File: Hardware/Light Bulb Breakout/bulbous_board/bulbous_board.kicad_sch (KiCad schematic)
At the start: 4 parts, among them Q1 NMOS, U1 Teensy4.1_DEV-16771

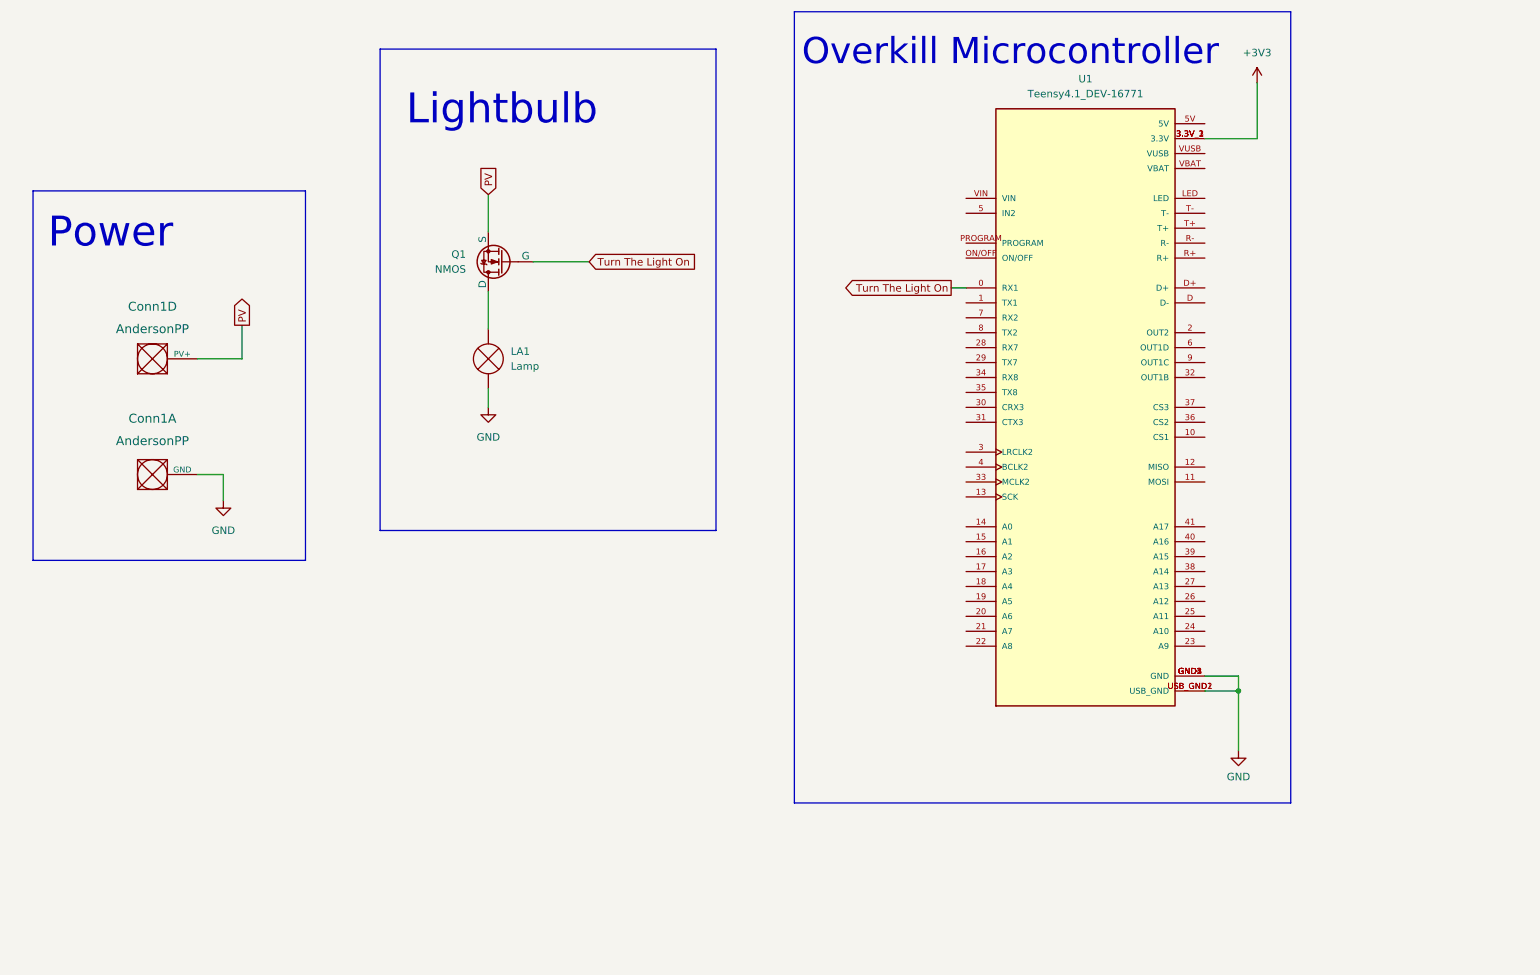
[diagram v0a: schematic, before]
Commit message: Amogus
Found out it is not a good idea to put 12 volts into the teensy and that's why we need an OKI. Also 2 pin connectors are a thing.
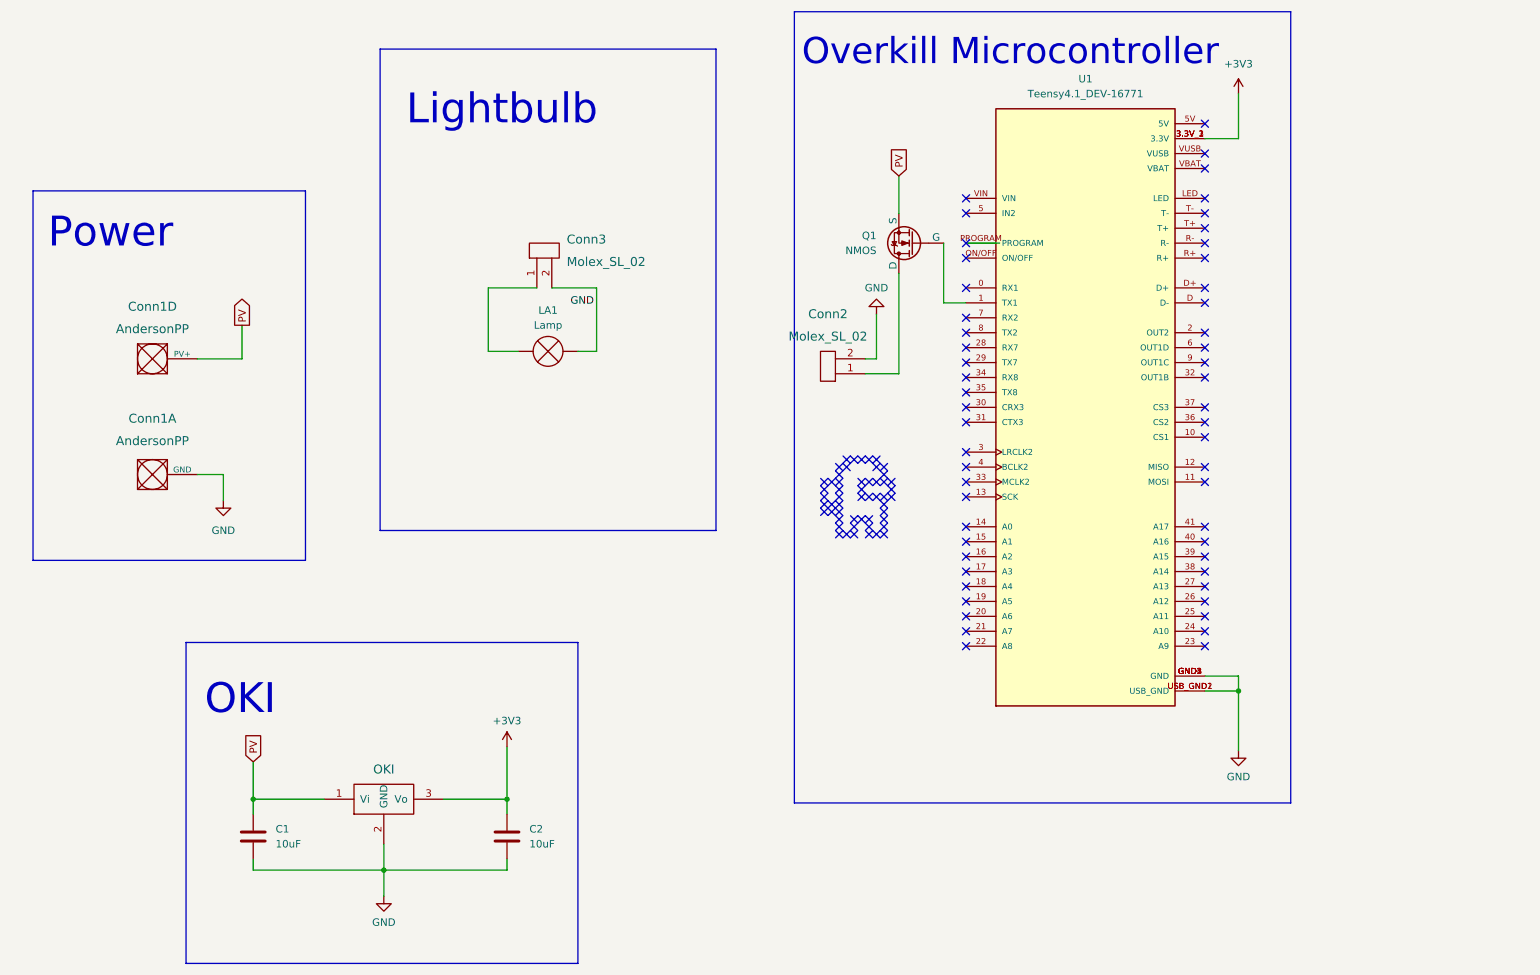
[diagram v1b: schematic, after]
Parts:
- added C1, C2: 10uF, Capacitor_SMD:C_0603_1608Metric_Pad1.08x0.95mm_HandSolder, symbol Device:C
- added Conn2, Conn3: Molex_SL_02, symbol MRDT_Connectors:Molex_SL_02
- added U2: OKI, MRDT_Devices:OKI_Horizontal, symbol MRDT_Devices:OKI
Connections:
- net +3V3: now also C2.1, U2.3 (Vo)
- net GND: now also C1.2, C2.2, Conn2.2, U2.2 (GND); no longer LA1.1 (-)
- net PV: now also C1.1, U2.1 (Vi)
- net at LA1.2 (+): now also Conn3.1; no longer Q1.1 (D)
- net at U1.1 (TX1): now also Q1.2 (G)
- net Turn The Light On: no longer names the net of U1.0 (RX1)
- net Turn The Light On: no longer Q1.2 (G)
- new net: Conn3.2, LA1.1 (-)
- new net: Conn2.1, Q1.1 (D)
- no-connect marks 0 -> 107
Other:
- note added: "OKI"
- moved on the sheet: LA1

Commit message: Amogus round 2
fixed a label because Derw said it was bad
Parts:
- removed unit 4 of Conn1
- added unit 5 of Conn1
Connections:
- net GND: now also Conn3.2, LA1.1 (-)
- net PV renamed +12V
- net +12V: now also Conn1.1
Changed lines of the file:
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@@
+    (stroke (width 0) (type default))
+  )
+  (wire (pts (xy 120.015 76.835) (xy 123.19 76.835))
     (stroke (width 0) (type default))
   )
@@
     (stroke (width 0) (type default))
   )
-  (wire (pts (xy 120.015 76.835) (xy 123.19 76.835))
+  (wire (pts (xy 76.835 153.035) (xy 64.77 153.035))
+    (stroke (width 0) (type default))
+  )
+  (wire (pts (xy 107.95 155.575) (xy 107.95 153.035))
+    (stroke (width 0) (type default))
+  )
+  (wire (pts (xy 123.19 76.835) (xy 123.19 66.04))
     (stroke (width 0) (type default))
   )
   (wire (pts (xy 55.245 78.105) (xy 62.865 78.105))
-    (stroke (width 0) (type default))
-  )
-  (wire (pts (xy 76.835 153.035) (xy 64.77 153.035))
-    (stroke (width 0) (type default))
-  )
-  (wire (pts (xy 107.95 155.575) (xy 107.95 153.035))
-    (stroke (width 0) (type default))
-  )
-  (wire (pts (xy 123.19 76.835) (xy 123.19 66.04))
     (stroke (width 0) (type default))
   )
@@
     (effects (font (size 5.08 5.08)) (justify left bottom))
   )
-  (label "GND" (at 118.745 69.215 0) (fields_autoplaced)
+  (label "GND" (at 115.57 66.04 0) (fields_autoplaced)
     (effects (font (size 1.27 1.27)) (justify left bottom))
   )
-  (global_label "PV" (shape input) (at 174.625 46.99 90) (fields_autoplaced)
-    (effects (font (size 1.27 1.27)) (justify left))
-    (property "Intersheetrefs" "${INTERSHEET_REFS}" (at 174.625 42.1465 90)
-      (effects (font (size 1.27 1.27)) (justify left) hide)
-    )
-  )
-  (global_label "PV" (shape output) (at 62.865 72.39 90) (fields_autoplaced)
-    (effects (font (size 1.27 1.27)) (justify left))
-    (property "Intersheetrefs" "${INTERSHEET_REFS}" (at 62.865 67.5465 90)
-      (effects (font (size 1.27 1.27)) (justify left) hide)
-    )
-  )
-  (global_label "PV" (shape input) (at 64.77 146.685 90) (fields_autoplaced)
-    (effects (font (size 1.27 1.27)) (justify left))
-    (property "Intersheetrefs" "${INTERSHEET_REFS}" (at 64.77 141.3412 90)
-      (effects (font (size 1.27 1.27)) (justify left) hide)
-    )
-  )
-  (symbol (lib_id "MRDT_Connectors:AndersonPP") (at 45.085 80.645 0) (unit 4)
-    (in_bom yes) (on_board yes) (dnp no) (fields_autoplaced)
-    (property "Reference" "Conn1" (at 47.625 69.215 0)
-      (effects (font (size 1.524 1.524)))
-    )
-    (property "Value" "AndersonPP" (at 47.625 73.025 0)
-      (effects (font (size 1.524 1.524)))
-    )
-    (property "Footprint" "" (at 41.275 94.615 0)
-      (effects (font (size 1.524 1.524)) hide)
-    )
-    (property "Datasheet" "" (at 41.275 94.615 0)
-      (effects (font (size 1.524 1.524)) hide)
-    )
-    (pin "1")
-    (pin "2")
-    (pin "3")
-    (pin "4")
-    (pin "1")
-    (instances
-      (project "bulbous_board"
-        (path "/049c3f09-c046-40c3-9872-e62b40667976"
-          (reference "Conn1") (unit 4)
+  (symbol (lib_id "power:+12V") (at 64.77 146.685 0) (unit 1)
+    (in_bom yes) (on_board yes) (dnp no) (fields_autoplaced)
+    (property "Reference" "#PWR09" (at 64.77 150.495 0)
+      (effects (font (size 1.27 1.27)) hide)
+    )
+    (property "Value" "+12V" (at 64.77 142.24 0)
+      (effects (font (size 1.27 1.27)))
+    )
+    (property "Footprint" "" (at 64.77 146.685 0)
+      (effects (font (size 1.27 1.27)) hide)
+    )
+    (property "Datasheet" "" (at 64.77 146.685 0)
+      (effects (font (size 1.27 1.27)) hide)
+    )
+    (pin "1")
+    (instances
+      (project "bulbous_board"
+        (path "/049c3f09-c046-40c3-9872-e62b40667976"
+          (reference "#PWR09") (unit 1)
         )
       )
@@
     )
   )
+  (symbol (lib_id "power:+12V") (at 62.865 72.39 0) (unit 1)
+    (in_bom yes) (on_board yes) (dnp no) (fields_autoplaced)
+    (property "Reference" "#PWR01" (at 62.865 76.2 0)
+      (effects (font (size 1.27 1.27)) hide)
+    )
+    (property "Value" "+12V" (at 62.865 67.31 0)
+      (effects (font (size 1.27 1.27)))
+    )
+    (property "Footprint" "" (at 62.865 72.39 0)
+      (effects (font (size 1.27 1.27)) hide)
+    )
+    (property "Datasheet" "" (at 62.865 72.39 0)
+      (effects (font (size 1.27 1.27)) hide)
+    )
+    (pin "1")
+    (instances
+      (project "bulbous_board"
+        (path "/049c3f09-c046-40c3-9872-e62b40667976"
+          (reference "#PWR01") (unit 1)
+        )
+      )
+    )
+  )
   (symbol (lib_id "Device:C") (at 107.95 159.385 0) (unit 1)
     (in_bom yes) (on_board yes) (dnp no) (fields_autoplaced)
@@
         (path "/88af529a-d884-4361-9125-c50b314779b3"
           (reference "C2") (unit 1)
+        )
+      )
+    )
+  )
+  (symbol (lib_id "MRDT_Connectors:AndersonPP") (at 45.085 80.645 0) (unit 5)
+    (in_bom yes) (on_board yes) (dnp no) (fields_autoplaced)
+    (property "Reference" "Conn1" (at 47.625 68.58 0)
+      (effects (font (size 1.524 1.524)))
+    )
+    (property "Value" "AndersonPP" (at 47.625 72.39 0)
+      (effects (font (size 1.524 1.524)))
+    )
+    (property "Footprint" "" (at 41.275 94.615 0)
+      (effects (font (size 1.524 1.524)) hide)
+    )
+    (property "Datasheet" "" (at 41.275 94.615 0)
+      (effects (font (size 1.524 1.524)) hide)
+    )
+    (pin "1")
+    (pin "2")
+    (pin "3")
+    (pin "4")
+    (pin "1")
+    (instances
+      (project "bulbous_board"
+        (path "/049c3f09-c046-40c3-9872-e62b40667976"
+          (reference "Conn1") (unit 5)
         )
       )
@@
         )
       )
+    )
+  )
+  (symbol (lib_id "power:+12V") (at 174.625 46.99 0) (unit 1)
+    (in_bom yes) (on_board yes) (dnp no) (fields_autoplaced)
+    (property "Reference" "#PWR08" (at 174.625 50.8 0)
+      (effects (font (size 1.27 1.27)) hide)
+    )
+    (property "Value" "+12V" (at 174.625 42.545 0)
+      (effects (font (size 1.27 1.27)))
+    )
+    (property "Footprint" "" (at 174.625 46.99 0)
+      (effects (font (size 1.27 1.27)) hide)
+    )
+    (property "Datasheet" "" (at 174.625 46.99 0)
+      (effects (font (size 1.27 1.27)) hide)
+    )
+    (pin "1")
+    (instances
+      (project "bulbous_board"
+        (path "/049c3f09-c046-40c3-9872-e62b40667976"
+          (reference "#PWR08") (unit 1)
+        )
+      )

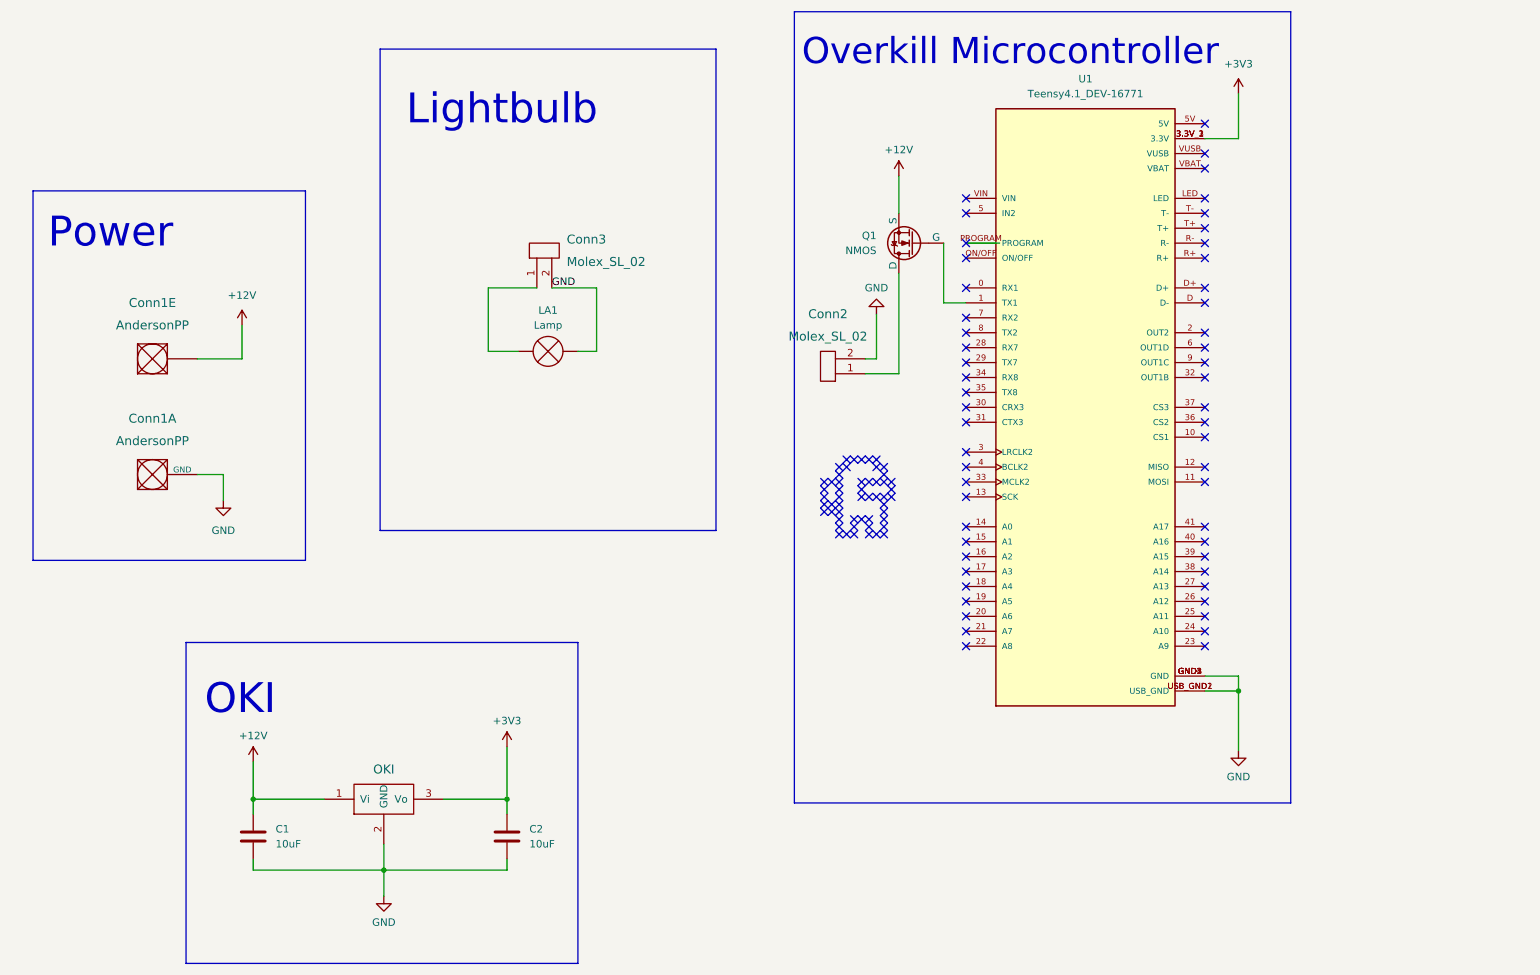
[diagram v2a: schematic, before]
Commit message: Created Stepper Symbol
TMC2208 Stepper Motor Driver and supporting circuitry.

Drew made me delete the amogus :,(
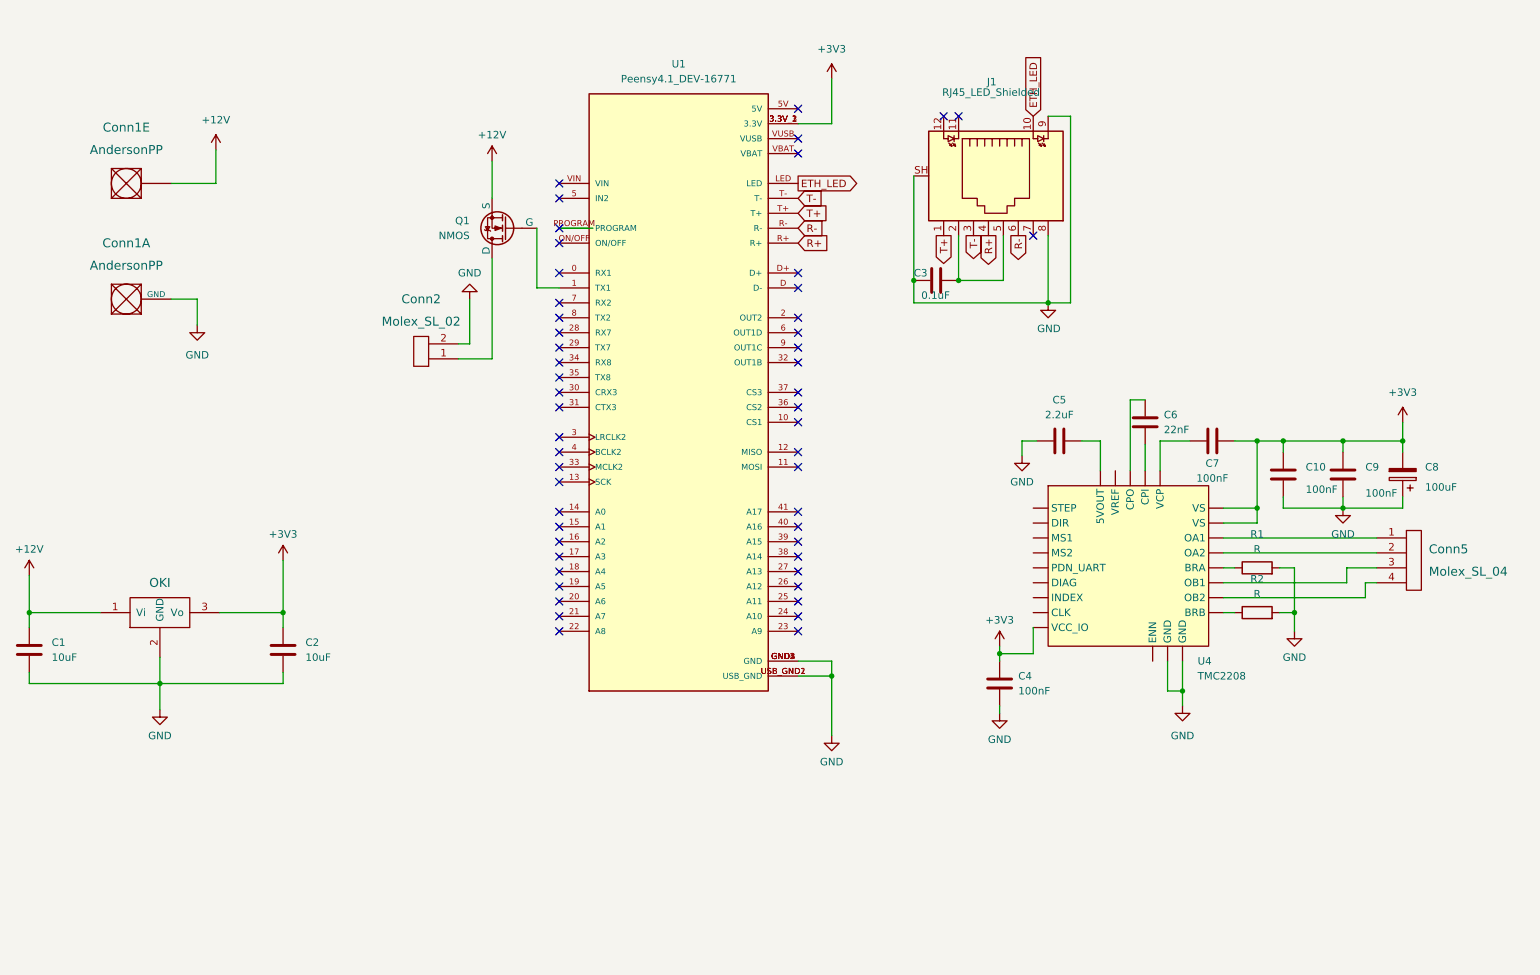
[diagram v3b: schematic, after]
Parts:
- removed Conn3: Molex_SL_02, symbol MRDT_Connectors:Molex_SL_02
- removed LA1: Lamp, symbol Device:Lamp
- added C10, C4, C7, C9: 100nF, symbol Device:C
- added C3: 0.1uF, Capacitor_SMD:C_0603_1608Metric_Pad1.08x0.95mm_HandSolder, symbol Device:C
- added C5: 2.2uF, symbol Device:C
- added C6: 22nF, symbol Device:C
- added C8: 100uF, symbol Device:C_Polarized
- added Conn5: Molex_SL_04, symbol MRDT_Connectors:Molex_SL_04
- added J1: RJ45_LED_Shielded, MRDT_Connectors:RJ45_Teensy, symbol Connector:RJ45_LED_Shielded
- added R1, R2: R, symbol Device:R
- added U4: TMC2208, symbol MRDT_Devices:TMC2208
- U1: value Teensy4.1_DEV-16771 -> Peensy4.1_DEV-16771
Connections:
- net +3V3: now also C10.1, C4.2, C7.2, C8.2, C9.1, U4. (VS)
- net GND: now also C10.2, C3.2, C4.1, C5.1, C8.1, C9.2, J1.8, J1.9, J1.SH, R1.2, R2.2, U4. (VS)
- net ETH_LED: now reaches U1.LED
- net ETH_LED: now also J1.10
- net R+: now reaches U1.R+
- net R+: now also J1.4
- net R-: now reaches U1.R-
- net R-: now also J1.6
- net T+: now reaches U1.T+
- net T+: now also J1.1
- net T-: now reaches U1.T-
- net T-: now also J1.3
- new net: R1.1, U4. (VS)
- new net: C3.1, J1.2, J1.5
- new net: C5.2, U4. (VS)
- new net: C6.1, U4. (VS)
- new net: C6.2, U4. (VS)
- new net: Conn5.1, U4. (VS)
- new net: Conn5.2, U4. (VS)
- new net: Conn5.3, U4. (VS)
- new net: Conn5.4, U4. (VS)
- new net: R2.1, U4. (VS)
- new net: C7.1, U4. (VS)
- no-connect marks 107 -> 52
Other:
- note removed: "Lightbulb"
- note removed: "OKI"
- note removed: "Overkill Microcontroller"
- note removed: "Power"
- moved on the sheet: C1, C2, Conn1A, Conn1E, Conn2, Q1, U1
